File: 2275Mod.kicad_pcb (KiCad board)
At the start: 2 copper layers, 121.1 x 57.5 mm, 41 parts, among them IC1 LTV-356T, J1 640388-8, J2 TagConnect_TC2030-MCP, J201 Conn_01x03_Male, K1 40.52.8.024.5000, K2 G5LE-14-CF_DC24, Q200 Q_NPN_Darlington_CBE, Q201 Q_NPN_Darlington_CBE, U1 LM340LAZ-5.0, U2 TCLT1600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

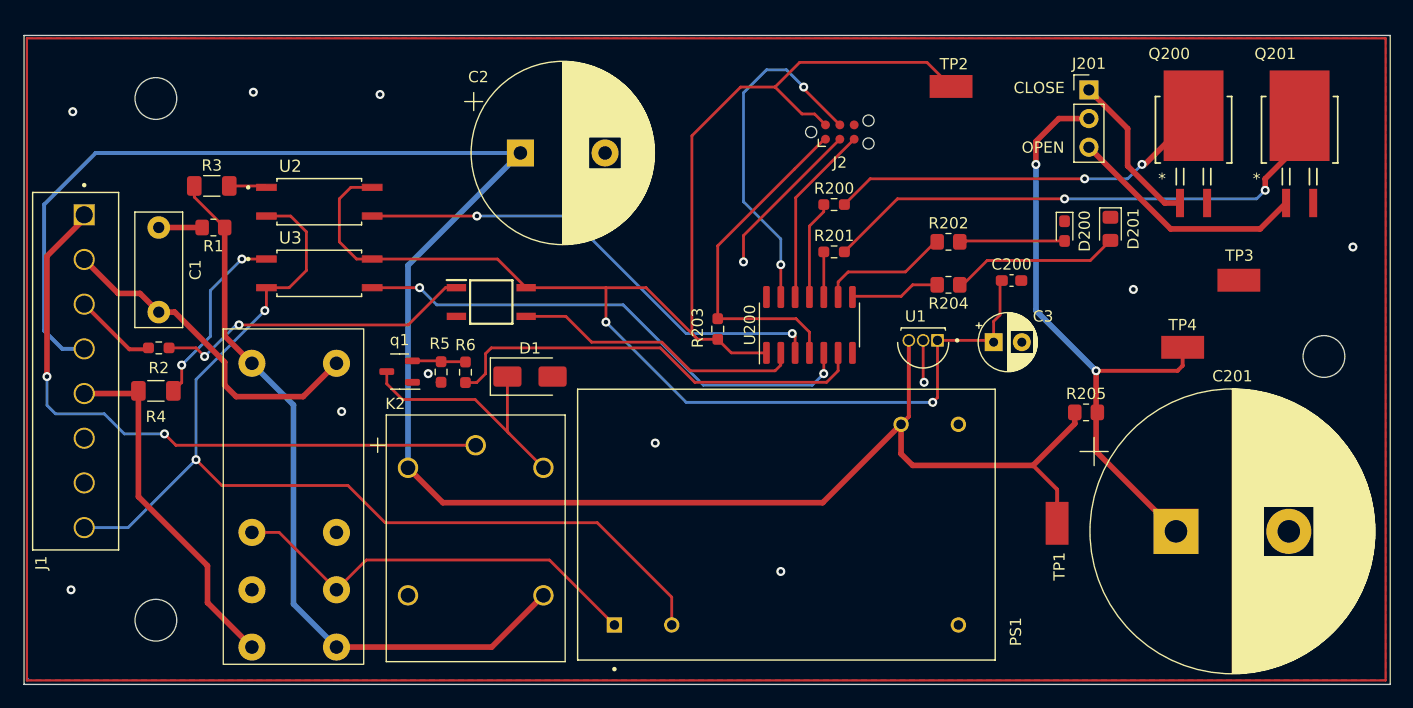
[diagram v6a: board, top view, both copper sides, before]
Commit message: move traces, move c200 next to micro, genral clean up
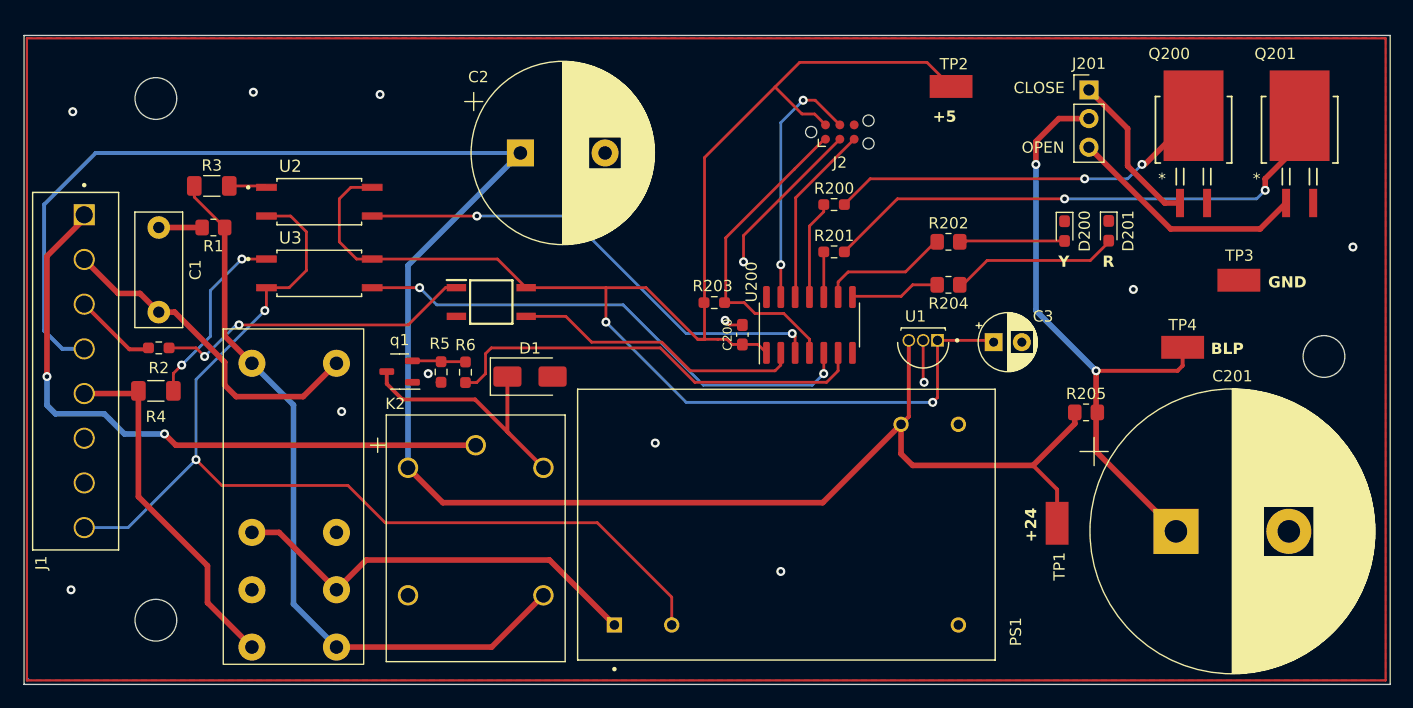
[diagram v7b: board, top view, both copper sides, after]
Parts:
- D201: footprint LED_SMD:LED_0805_2012Metric_Pad1.15x1.40mm_HandSolder -> LED_SMD:LED_0603_1608Metric_Pad1.05x0.95mm_HandSolder
- moved C200 24.3 mm to (165.5, 97.4), turned to 90 degrees
- moved R203 2.36 mm to (163.0, 94.5), turned to 180 degrees
- moved D201 0.23 mm to (198.0, 88.2)
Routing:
- net /MCU/DAT: track 31.0 -> 22.4 mm
- net +5V: track 151.1 -> 143.5 mm
- net /MCU/MCLR: track 30.4 -> 28.2 mm
- net GND: track 18.5 -> 20.2 mm, vias 12 -> 13
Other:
- board text added: "+24"
- board text added: "+5"
- board text added: "BLP"
- board text added: "GND"
- board text added: "R"
- board text added: "Y"

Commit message: corrected q200 and q201 footprints
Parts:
- C1: footprint Capacitor_THT:C_Rect_L10.0mm_W4.0mm_P7.50mm_MKS4 -> Capacitor_THT:C_Rect_L9.0mm_W3.8mm_P7.50mm_MKT
- Q200, Q201: footprint AAA_JH:TRANS_2SD1918_ROM-M -> Package_TO_SOT_SMD:SOT-223-3_TabPin2
- moved C1 4.36 mm to (113.1, 83.6)
- moved Q201 1.05 mm to (215.4, 78.3), turned to 90 degrees
- moved Q200 0.79 mm to (205.5, 78.4), turned to 90 degrees
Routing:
- net /L2: track 29.8 -> 35.9 mm
- net Net-(Q200-B): track 34.2 -> 40.2 mm
- net Net-(Q201-B): track 47.4 -> 52.3 mm
- net /MCU/Close: track 14.2 -> 9.41 mm
- net Net-(C1-Pad1): track 3.84 -> 7.38 mm
- net /MCU/Open: track 21.4 -> 22.1 mm
